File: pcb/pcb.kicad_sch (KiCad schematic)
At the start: 15 parts, among them J1 Connector

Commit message: buck converter and updates
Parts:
- removed J1: Connector, Connector_JST:JST_PH_S4B-PH-K_1x04_P2.00mm_Horizontal, symbol Connector:Conn_01x04_Pin
- removed TP1: LORA_SCK, TestPoint:TestPoint_Pad_2.0x2.0mm, symbol Connector:TestPoint
- removed TP2: LORA_MOSI, TestPoint:TestPoint_Pad_2.0x2.0mm, symbol Connector:TestPoint
- removed TP3: LORA_MISO, TestPoint:TestPoint_Pad_2.0x2.0mm, symbol Connector:TestPoint
- removed TP4: LORA_CS, TestPoint:TestPoint_Pad_2.0x2.0mm, symbol Connector:TestPoint
- removed TP5: BT_SCK, TestPoint:TestPoint_Pad_2.0x2.0mm, symbol Connector:TestPoint
- removed TP6: BT_MOSI, TestPoint:TestPoint_Pad_2.0x2.0mm, symbol Connector:TestPoint
- removed TP7: BT_MISO, TestPoint:TestPoint_Pad_2.0x2.0mm, symbol Connector:TestPoint
- removed TP8: BT_CS, TestPoint:TestPoint_Pad_2.0x2.0mm, symbol Connector:TestPoint
- added J1: Battery, Connector_JST:JST_GH_SM02B-GHS-TB_1x02-1MP_P1.25mm_Horizontal, symbol Connector:Conn_01x02_Pin
- added J4: LoRa Test Conn, Connector_JST:JST_GH_SM04B-GHS-TB_1x04-1MP_P1.25mm_Horizontal, symbol Connector:Conn_01x04_Pin
- added J5: BT Test Conn, Connector_JST:JST_GH_SM04B-GHS-TB_1x04-1MP_P1.25mm_Horizontal, symbol Connector:Conn_01x04_Pin
- added J6: I2C 1, Connector_JST:JST_GH_SM04B-GHS-TB_1x04-1MP_P1.25mm_Horizontal, symbol Connector:Conn_01x04_Pin
- added J7: I2C 2, Connector_JST:JST_GH_SM04B-GHS-TB_1x04-1MP_P1.25mm_Horizontal, symbol Connector:Conn_01x04_Pin
- added J8: UART, Connector_JST:JST_GH_SM02B-GHS-TB_1x02-1MP_P1.25mm_Horizontal, symbol Connector:Conn_01x02_Pin
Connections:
- net BT_CS: now also J5.1 (Pin_1)
- net BT_MISO: now also J5.2 (Pin_2)
- net BT_MOSI: now also J5.3 (Pin_3)
- net BT_SCK: now also J5.4 (Pin_4)
- net GND: now also J1.1 (Pin_1), J6.1 (Pin_1), J7.1 (Pin_1)
- net LORA_CS: now also J4.1 (Pin_1)
- net LORA_MISO: now also J4.2 (Pin_2)
- net LORA_MOSI: now also J4.3 (Pin_3)
- net LORA_SCK: now also J4.4 (Pin_4)
- net UART_RX: now also J8.1 (Pin_1)
- net UART_TX: now also J8.2 (Pin_2)
- net V_{IN}: now also J1.2 (Pin_2)
- new net +5V: J6.4 (Pin_4), J7.4 (Pin_4)
- new net I2C1_SCL: J6.2 (Pin_2)
- new net I2C1_SDA: J6.3 (Pin_3)
- new net I2C2_SCL: J7.2 (Pin_2)
- new net I2C2_SDA: J7.3 (Pin_3)
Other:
- sheet Power ports: added +5V; removed none
- note added: "V_{IN} is 2S [6V,8.4V] (7V Nominal)"
- note removed: "V_{IN} can be from 3.3V to 5V * Direct powering from a 1S LiPo may run into issues with LDOs not working when voltage runs below a nominal ~3.5V"

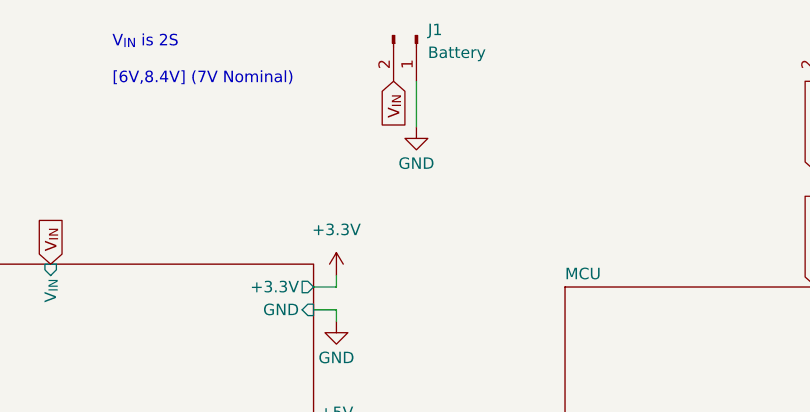
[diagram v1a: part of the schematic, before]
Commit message: switch TCXO, laid out from ref design from nordic
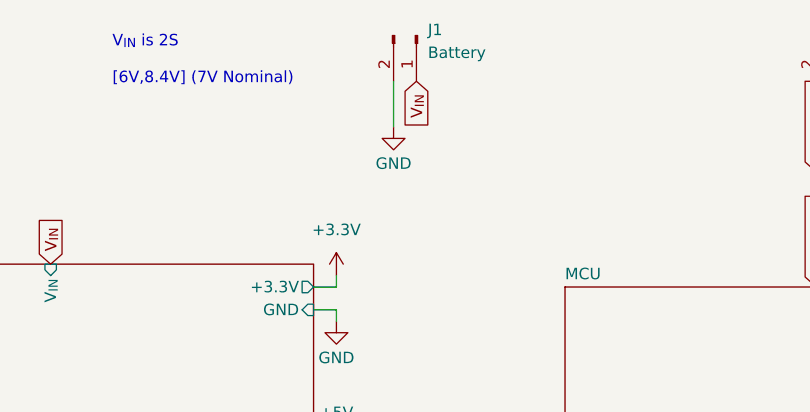
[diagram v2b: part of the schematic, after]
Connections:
- net GND: now also J1.2 (Pin_2); no longer J1.1 (Pin_1)
- net V_{IN}: now also J1.1 (Pin_1); no longer J1.2 (Pin_2)
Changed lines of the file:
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@@
+	(wire
+		(pts
+			(xy 86.36 30.48) (xy 86.36 25.4)
+		)
+		(stroke
+			(width 0)
+			(type default)
+		)
+	)
 	(wire
 		(pts
@@
 		(pts
 			(xy 48.26 172.72) (xy 48.26 175.26)
-		)
-		(stroke
-			(width 0)
-			(type default)
-		)
-	)
-	(wire
-		(pts
-			(xy 88.9 30.48) (xy 88.9 25.4)
 		)
 		(stroke
@@
 		)
 	)
+	(global_label "V_{IN}"
+		(shape input)
+		(at 88.9 25.4 270)
+		(fields_autoplaced yes)
+		(effects
+			(font
+				(size 1.27 1.27)
+			)
+			(justify right)
+		)
+		(property "Intersheetrefs" "${INTERSHEET_REFS}"
+			(at 88.9 31.0728 90)
+			(hide yes)
+			(show_name no)
+			(do_not_autoplace no)
+			(effects
+				(font
+					(size 1.27 1.27)
+				)
+				(justify right)
+			)
+		)
+	)
 	(global_label "UART_TX"
 		(shape output)
@@
 		)
 	)
-	(global_label "V_{IN}"
-		(shape input)
-		(at 86.36 25.4 270)
-		(fields_autoplaced yes)
-		(effects
-			(font
-				(size 1.27 1.27)
-			)
-			(justify right)
-		)
-		(property "Intersheetrefs" "${INTERSHEET_REFS}"
-			(at 86.36 31.0728 90)
-			(hide yes)
-			(show_name no)
-			(do_not_autoplace no)
-			(effects
-				(font
-					(size 1.27 1.27)
-				)
-				(justify right)
-			)
-		)
-	)
 	(global_label "UART_TX"
 		(shape input)
@@
 				)
 				(justify left)
+			)
+		)
+	)
+	(symbol
+		(lib_id "power:GND")
+		(at 86.36 30.48 0)
+		(unit 1)
+		(body_style 1)
+		(exclude_from_sim no)
+		(in_bom yes)
+		(on_board yes)
+		(in_pos_files yes)
+		(dnp no)
+		(property "Reference" "#PWR080"
+			(at 86.36 36.83 0)
+			(hide yes)
+			(show_name no)
+			(do_not_autoplace no)
+			(effects
+				(font
+					(size 1.27 1.27)
+				)
+			)
+		)
+		(property "Value" "GND"
+			(at 86.36 34.544 0)
+			(show_name no)
+			(do_not_autoplace no)
+			(effects
+				(font
+					(size 1.27 1.27)
+				)
+			)
+		)
+		(property "Footprint" ""
+			(at 86.36 30.48 0)
+			(hide yes)
+			(show_name no)
+			(do_not_autoplace no)
+			(effects
+				(font
+					(size 1.27 1.27)
+				)
+			)
+		)
+		(property "Datasheet" ""
+			(at 86.36 30.48 0)
+			(hide yes)
+			(show_name no)
+			(do_not_autoplace no)
+			(effects
+				(font
+					(size 1.27 1.27)
+				)
+			)
+		)
+		(property "Description" "Power symbol creates a global label with name \"GND\" , ground"
+			(at 86.36 30.48 0)
+			(hide yes)
+			(show_name no)
+			(do_not_autoplace no)
+			(effects
+				(font
+					(size 1.27 1.27)
+				)
+			)
+		)
+		(pin "1"
+		)
+		(instances
+			(project "pcb"
+				(path "/52b1b5de-c493-4cfe-b90b-d072cb2fb98d"
+					(reference "#PWR080")
+					(unit 1)
+				)
 			)
 		)
@@
 					(unit 1)
 				)
-			)
-		)
-	)
-	(symbol
-		(lib_id "power:GND")
-		(at 88.9 30.48 0)
-		(unit 1)
-		(body_style 1)
-		(exclude_from_sim no)
-		(in_bom yes)
-		(on_board yes)
-		(in_pos_files yes)
-		(dnp no)
-		(property "Reference" "#PWR080"
-			(at 88.9 36.83 0)
-			(hide yes)
-			(show_name no)
-			(do_not_autoplace no)
-			(effects
-				(font
-					(size 1.27 1.27)
-				)
-			)
-		)
-		(property "Value" "GND"
-			(at 88.9 34.544 0)
-			(show_name no)
-			(do_not_autoplace no)
-			(effects
-				(font
-					(size 1.27 1.27)
-				)
-			)
-		)
-		(property "Footprint" ""
-			(at 88.9 30.48 0)
-			(hide yes)
-			(show_name no)
-			(do_not_autoplace no)
-			(effects
-				(font
-					(size 1.27 1.27)
-				)
-			)
-		)
-		(property "Datasheet" ""
-			(at 88.9 30.48 0)
-			(hide yes)
-			(show_name no)
-			(do_not_autoplace no)
-			(effects
-				(font
-					(size 1.27 1.27)
-				)
-			)
-		)
-		(property "Description" "Power symbol creates a global label with name \"GND\" , ground"
-			(at 88.9 30.48 0)
-			(hide yes)
-			(show_name no)
-			(do_not_autoplace no)
-			(effects
-				(font
-					(size 1.27 1.27)
-				)
-			)
-		)
-		(pin "1"
-		)
-		(instances
-			(project "pcb"
-				(path "/52b1b5de-c493-4cfe-b90b-d072cb2fb98d"
-					(reference "#PWR080")
-					(unit 1)
-				)

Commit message: V2
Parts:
- added R18, R19, R20, R21: 5.1k, Resistor_SMD:R_0603_1608Metric, symbol Device:R_Small
- J3: renamed from J6; value I2C 1 -> I2C 2
- J6: renamed from J7; value I2C 2 -> I2C 1
- TP1: renamed from TP9; footprint TestPoint:TestPoint_Pad_2.0x2.0mm -> TestPoint:TestPoint_Pad_D1.0mm
- TP2: renamed from TP10; footprint TestPoint:TestPoint_Pad_2.0x2.0mm -> TestPoint:TestPoint_Pad_D1.0mm
- renumbered J8 to J2
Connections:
- net +3.3V: now also R18.1, R19.1, R20.1, R21.1
- net I2C1_SCL: now also J6.2 (Pin_2), R19.2; no longer J3.2 (Pin_2)
- net I2C1_SDA: now also J6.3 (Pin_3), R18.2; no longer J3.3 (Pin_3)
- net I2C2_SCL: now also J3.2 (Pin_2), R20.2; no longer J6.2 (Pin_2)
- net I2C2_SDA: now also J3.3 (Pin_3), R21.2; no longer J6.3 (Pin_3)
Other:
- sheet MCU ports: added I2C1_SCL, I2C1_SDA, I2C2_SCL, I2C2_SDA; removed none
- note added: "5.1k for BOM consolidation, standard is 4.7k for regular speed i^{2}c"
- moved on the sheet: J3

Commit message: revision 3
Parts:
- removed J2: UART, Connector_JST:JST_GH_SM02B-GHS-TB_1x02-1MP_P1.25mm_Horizontal, symbol Connector:Conn_01x02_Pin
- removed J4: LoRa Test Conn, Connector_JST:JST_GH_SM04B-GHS-TB_1x04-1MP_P1.25mm_Horizontal, symbol Connector:Conn_01x04_Pin
- removed J5: BT Test Conn, Connector_JST:JST_GH_SM04B-GHS-TB_1x04-1MP_P1.25mm_Horizontal, symbol Connector:Conn_01x04_Pin
- removed TP1: UART_TX, TestPoint:TestPoint_Pad_D1.0mm, symbol Connector:TestPoint
- removed TP2: UART_RX, TestPoint:TestPoint_Pad_D1.0mm, symbol Connector:TestPoint
- added J4: LoRa Debug, Connector_PinHeader_2.54mm:PinHeader_2x03_P2.54mm_Vertical, symbol Connector_Generic:Conn_02x03_Odd_Even
- added J5: BT Debug, Connector_PinHeader_2.54mm:PinHeader_2x02_P2.54mm_Vertical, symbol Connector_Generic:Conn_02x02_Odd_Even
- added J9: UART, Connector_JST:JST_GH_SM04B-GHS-TB_1x04-1MP_P1.25mm_Horizontal, symbol Connector:Conn_01x04_Pin
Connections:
- net +5V: now also J9.1 (Pin_1)
- net BT_CS: now also J5.4 (Pin_4)
- net BT_MISO: now also J5.2 (Pin_2)
- net BT_MOSI: now also J5.3 (Pin_3)
- net BT_SCK: now also J5.1 (Pin_1)
- net GND: now also J9.4 (Pin_4)
- net LORA_CS: now also J4.2 (Pin_2)
- net LORA_MISO: now also J4.5 (Pin_5)
- net LORA_MOSI: now also J4.3 (Pin_3)
- net LORA_SCK: now also J4.1 (Pin_1)
- net UART_RX: now also J9.2 (Pin_2)
- net UART_TX: now also J9.3 (Pin_3)
- new net DIO1: J4.6 (Pin_6)
- new net LORA_BUSY: J4.4 (Pin_4)
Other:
- sheet Power ports: added VBUS; removed none
